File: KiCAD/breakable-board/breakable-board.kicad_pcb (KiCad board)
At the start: 2 copper layers, 76.2 x 99.1 mm, 50 parts, among them J1 POWER1, J10 TQFP-32-2, J11 3.3V Out, J12 Power In, J13 5V Out, J14 GND, J15 SSOP-20-1, J16 SSOP-20-2, J17 I2C, J18 UART, J2 POWER3, J3 OUT1, J4 POWER2, J5 OUT3, J6 OUT2, J7 SOIC-14-1, J8 SOIC-14-2, J9 TQFP-32-1, SW1 Trigger, SW2 RESET, U1 LM555xN, U2 LM555xN, U3 LM555xN, U4 Package_SOIC-14, U5 Package_TQFP-32, U6 AMS1117-5.0, U7 AMS1117-3.3, U8 PIC16F1508-ISS

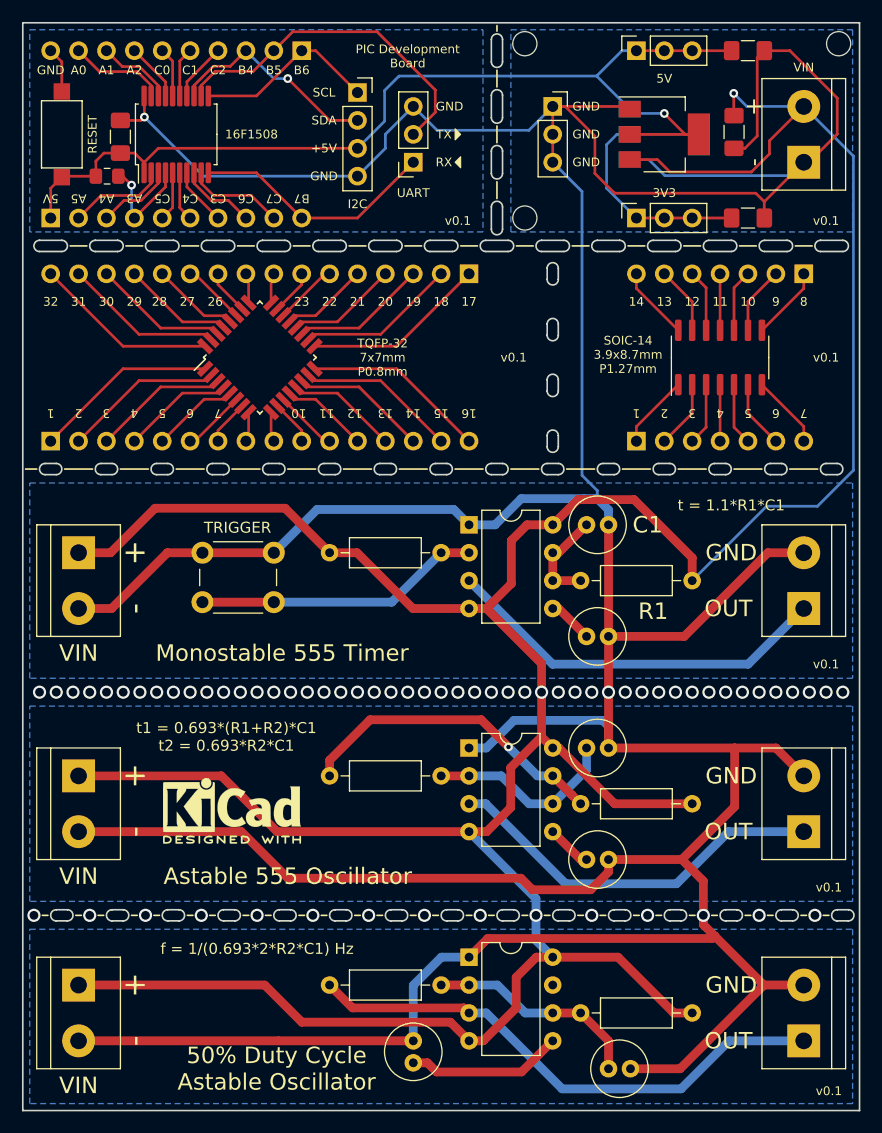
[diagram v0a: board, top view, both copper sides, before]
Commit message: Change hole size.
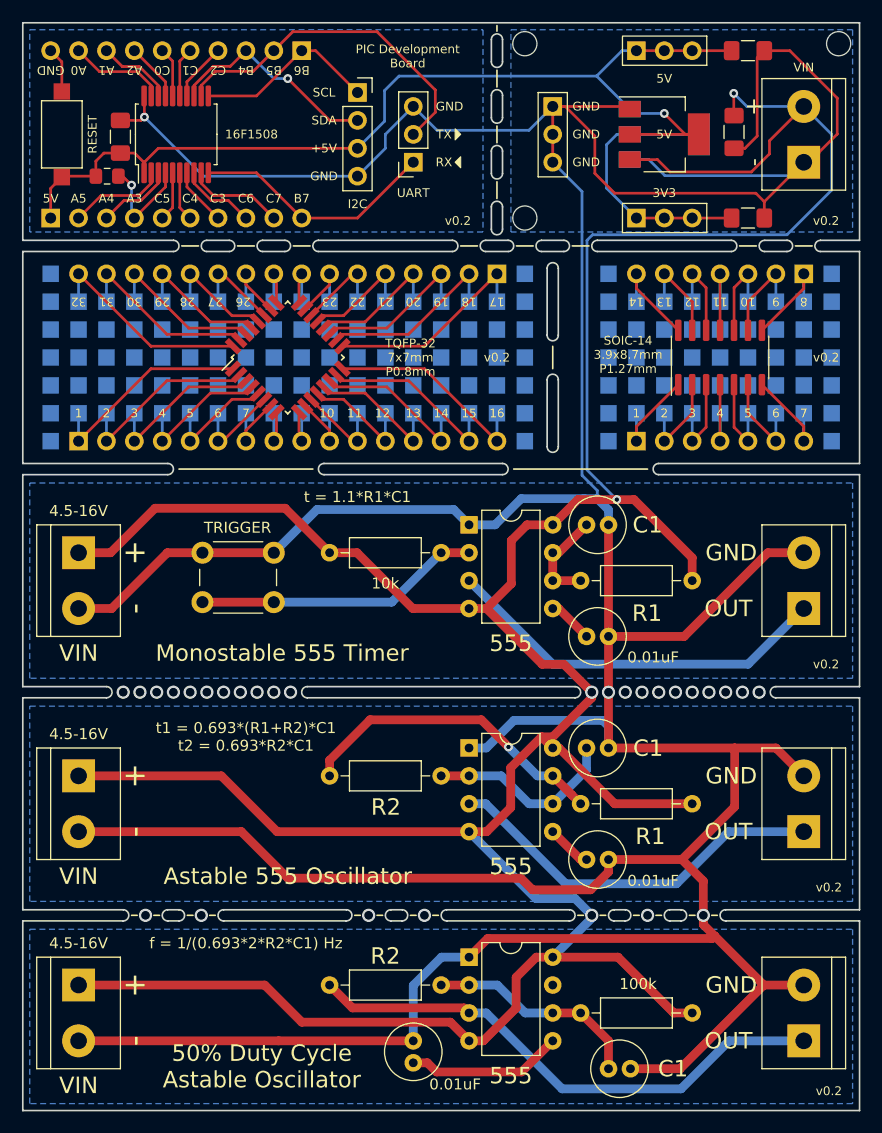
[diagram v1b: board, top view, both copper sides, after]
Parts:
- added .: ., TestPoint:TestPoint_Pad_1.5x1.5mm, B.Cu at (83.8, 58.4)
- added .: ., TestPoint:TestPoint_Pad_1.5x1.5mm, B.Cu at (91.4, 48.3)
- added .: ., TestPoint:TestPoint_Pad_1.5x1.5mm, B.Cu at (66.0, 53.3)
- added .: ., TestPoint:TestPoint_Pad_1.5x1.5mm, B.Cu at (66.0, 55.9)
- added .: ., TestPoint:TestPoint_Pad_1.5x1.5mm, B.Cu at (61.0, 53.3)
- added .: ., TestPoint:TestPoint_Pad_1.5x1.5mm, B.Cu at (58.4, 50.8)
- added .: ., TestPoint:TestPoint_Pad_1.5x1.5mm, B.Cu at (66.0, 50.8)
- added .: ., TestPoint:TestPoint_Pad_1.5x1.5mm, B.Cu at (63.5, 50.8)
- added .: ., TestPoint:TestPoint_Pad_1.5x1.5mm, B.Cu at (55.9, 55.9)
- added .: ., TestPoint:TestPoint_Pad_1.5x1.5mm, B.Cu at (58.4, 53.3)
- added .: ., TestPoint:TestPoint_Pad_1.5x1.5mm, B.Cu at (61.0, 55.9)
- added .: ., TestPoint:TestPoint_Pad_1.5x1.5mm, B.Cu at (63.5, 53.3)
- added .: ., TestPoint:TestPoint_Pad_1.5x1.5mm, B.Cu at (83.8, 48.3)
- added .: ., TestPoint:TestPoint_Pad_1.5x1.5mm, B.Cu at (58.4, 55.9)
- added .: ., TestPoint:TestPoint_Pad_1.5x1.5mm, B.Cu at (55.9, 53.3)
- added .: ., TestPoint:TestPoint_Pad_1.5x1.5mm, B.Cu at (61.0, 50.8)
- added .: ., TestPoint:TestPoint_Pad_1.5x1.5mm, B.Cu at (55.9, 50.8)
- added .: ., TestPoint:TestPoint_Pad_1.5x1.5mm, B.Cu at (50.8, 53.3)
- added .: ., TestPoint:TestPoint_Pad_1.5x1.5mm, B.Cu at (50.8, 55.9)
- added .: ., TestPoint:TestPoint_Pad_1.5x1.5mm, B.Cu at (53.3, 53.3)
- added .: ., TestPoint:TestPoint_Pad_1.5x1.5mm, B.Cu at (53.3, 55.9)
- added .: ., TestPoint:TestPoint_Pad_1.5x1.5mm, B.Cu at (53.3, 50.8)
- added .: ., TestPoint:TestPoint_Pad_1.5x1.5mm, B.Cu at (50.8, 50.8)
- added .: ., TestPoint:TestPoint_Pad_1.5x1.5mm, B.Cu at (94.0, 48.3)
- added .: ., TestPoint:TestPoint_Pad_1.5x1.5mm, B.Cu at (48.3, 53.3)
- added .: ., TestPoint:TestPoint_Pad_1.5x1.5mm, B.Cu at (45.7, 53.3)
- added .: ., TestPoint:TestPoint_Pad_1.5x1.5mm, B.Cu at (43.2, 50.8)
- added .: ., TestPoint:TestPoint_Pad_1.5x1.5mm, B.Cu at (45.7, 55.9)
- added .: ., TestPoint:TestPoint_Pad_1.5x1.5mm, B.Cu at (43.2, 55.9)
- added .: ., TestPoint:TestPoint_Pad_1.5x1.5mm, B.Cu at (43.2, 53.3)
- added .: ., TestPoint:TestPoint_Pad_1.5x1.5mm, B.Cu at (48.3, 50.8)
- added .: ., TestPoint:TestPoint_Pad_1.5x1.5mm, B.Cu at (48.3, 55.9)
- added .: ., TestPoint:TestPoint_Pad_1.5x1.5mm, B.Cu at (45.7, 50.8)
- added .: ., TestPoint:TestPoint_Pad_1.5x1.5mm, B.Cu at (40.6, 53.3)
- added .: ., TestPoint:TestPoint_Pad_1.5x1.5mm, B.Cu at (88.9, 48.3)
- added .: ., TestPoint:TestPoint_Pad_1.5x1.5mm, B.Cu at (40.6, 55.9)
- added .: ., TestPoint:TestPoint_Pad_1.5x1.5mm, B.Cu at (40.6, 50.8)
- added .: ., TestPoint:TestPoint_Pad_1.5x1.5mm, B.Cu at (38.1, 53.3)
- added .: ., TestPoint:TestPoint_Pad_1.5x1.5mm, B.Cu at (38.1, 50.8)
- added .: ., TestPoint:TestPoint_Pad_1.5x1.5mm, B.Cu at (38.1, 55.9)
- added .: ., TestPoint:TestPoint_Pad_1.5x1.5mm, B.Cu at (35.6, 55.9)
- added .: ., TestPoint:TestPoint_Pad_1.5x1.5mm, B.Cu at (33.0, 55.9)
- added .: ., TestPoint:TestPoint_Pad_1.5x1.5mm, B.Cu at (30.5, 55.9)
- added .: ., TestPoint:TestPoint_Pad_1.5x1.5mm, B.Cu at (30.5, 53.3)
- added .: ., TestPoint:TestPoint_Pad_1.5x1.5mm, B.Cu at (35.6, 53.3)
- added .: ., TestPoint:TestPoint_Pad_1.5x1.5mm, B.Cu at (86.4, 48.3)
- added .: ., TestPoint:TestPoint_Pad_1.5x1.5mm, B.Cu at (33.0, 53.3)
- added .: ., TestPoint:TestPoint_Pad_1.5x1.5mm, B.Cu at (35.6, 50.8)
- added .: ., TestPoint:TestPoint_Pad_1.5x1.5mm, B.Cu at (33.0, 50.8)
- added .: ., TestPoint:TestPoint_Pad_1.5x1.5mm, B.Cu at (30.5, 50.8)
- added .: ., TestPoint:TestPoint_Pad_1.5x1.5mm, B.Cu at (66.0, 58.4)
- added .: ., TestPoint:TestPoint_Pad_1.5x1.5mm, B.Cu at (58.4, 58.4)
- added .: ., TestPoint:TestPoint_Pad_1.5x1.5mm, B.Cu at (45.7, 58.4)
- added .: ., TestPoint:TestPoint_Pad_1.5x1.5mm, B.Cu at (68.6, 58.4)
- added .: ., TestPoint:TestPoint_Pad_1.5x1.5mm, B.Cu at (50.8, 58.4)
- added .: ., TestPoint:TestPoint_Pad_1.5x1.5mm, B.Cu at (91.4, 58.4)
- added .: ., TestPoint:TestPoint_Pad_1.5x1.5mm, B.Cu at (43.2, 58.4)
- added .: ., TestPoint:TestPoint_Pad_1.5x1.5mm, B.Cu at (48.3, 58.4)
- added .: ., TestPoint:TestPoint_Pad_1.5x1.5mm, B.Cu at (53.3, 58.4)
- added .: ., TestPoint:TestPoint_Pad_1.5x1.5mm, B.Cu at (33.0, 58.4)
- added .: ., TestPoint:TestPoint_Pad_1.5x1.5mm, B.Cu at (63.5, 58.4)
- added .: ., TestPoint:TestPoint_Pad_1.5x1.5mm, B.Cu at (61.0, 58.4)
- added .: ., TestPoint:TestPoint_Pad_1.5x1.5mm, B.Cu at (55.9, 58.4)
- added .: ., TestPoint:TestPoint_Pad_1.5x1.5mm, B.Cu at (40.6, 58.4)
- added .: ., TestPoint:TestPoint_Pad_1.5x1.5mm, B.Cu at (38.1, 58.4)
- added .: ., TestPoint:TestPoint_Pad_1.5x1.5mm, B.Cu at (30.5, 58.4)
- added .: ., TestPoint:TestPoint_Pad_1.5x1.5mm, B.Cu at (88.9, 58.4)
- added .: ., TestPoint:TestPoint_Pad_1.5x1.5mm, B.Cu at (35.6, 58.4)
- added .: ., TestPoint:TestPoint_Pad_1.5x1.5mm, B.Cu at (68.6, 48.3)
- added .: ., TestPoint:TestPoint_Pad_1.5x1.5mm, B.Cu at (45.7, 48.3)
- added .: ., TestPoint:TestPoint_Pad_1.5x1.5mm, B.Cu at (53.3, 48.3)
- added .: ., TestPoint:TestPoint_Pad_1.5x1.5mm, B.Cu at (50.8, 48.3)
- added .: ., TestPoint:TestPoint_Pad_1.5x1.5mm, B.Cu at (48.3, 48.3)
- added .: ., TestPoint:TestPoint_Pad_1.5x1.5mm, B.Cu at (43.2, 48.3)
- added .: ., TestPoint:TestPoint_Pad_1.5x1.5mm, B.Cu at (58.4, 48.3)
- added .: ., TestPoint:TestPoint_Pad_1.5x1.5mm, B.Cu at (66.0, 48.3)
- added .: ., TestPoint:TestPoint_Pad_1.5x1.5mm, B.Cu at (63.5, 48.3)
- added .: ., TestPoint:TestPoint_Pad_1.5x1.5mm, B.Cu at (94.0, 58.4)
- added .: ., TestPoint:TestPoint_Pad_1.5x1.5mm, B.Cu at (61.0, 48.3)
- added .: ., TestPoint:TestPoint_Pad_1.5x1.5mm, B.Cu at (55.9, 48.3)
- added .: ., TestPoint:TestPoint_Pad_1.5x1.5mm, B.Cu at (40.6, 48.3)
- added .: ., TestPoint:TestPoint_Pad_1.5x1.5mm, B.Cu at (38.1, 48.3)
- added .: ., TestPoint:TestPoint_Pad_1.5x1.5mm, B.Cu at (30.5, 48.3)
- added .: ., TestPoint:TestPoint_Pad_1.5x1.5mm, B.Cu at (35.6, 48.3)
- added .: ., TestPoint:TestPoint_Pad_1.5x1.5mm, B.Cu at (33.0, 48.3)
- added .: ., TestPoint:TestPoint_Pad_1.5x1.5mm, B.Cu at (78.7, 55.9)
- added .: ., TestPoint:TestPoint_Pad_1.5x1.5mm, B.Cu at (78.7, 50.8)
- added .: ., TestPoint:TestPoint_Pad_1.5x1.5mm, B.Cu at (78.7, 53.3)
- added .: ., TestPoint:TestPoint_Pad_1.5x1.5mm, B.Cu at (81.3, 58.4)
- added .: ., TestPoint:TestPoint_Pad_1.5x1.5mm, B.Cu at (78.7, 45.7)
- added .: ., TestPoint:TestPoint_Pad_1.5x1.5mm, B.Cu at (78.7, 48.3)
- added .: ., TestPoint:TestPoint_Pad_1.5x1.5mm, B.Cu at (78.7, 58.4)
- added .: ., TestPoint:TestPoint_Pad_1.5x1.5mm, B.Cu at (78.7, 61.0)
- added .: ., TestPoint:TestPoint_Pad_1.5x1.5mm, B.Cu at (99.1, 61.0)
- added .: ., TestPoint:TestPoint_Pad_1.5x1.5mm, B.Cu at (99.1, 58.4)
- added .: ., TestPoint:TestPoint_Pad_1.5x1.5mm, B.Cu at (99.1, 45.7)
- added .: ., TestPoint:TestPoint_Pad_1.5x1.5mm, B.Cu at (99.1, 48.3)
- added .: ., TestPoint:TestPoint_Pad_1.5x1.5mm, B.Cu at (99.1, 50.8)
- added .: ., TestPoint:TestPoint_Pad_1.5x1.5mm, B.Cu at (99.1, 53.3)
- added .: ., TestPoint:TestPoint_Pad_1.5x1.5mm, B.Cu at (96.5, 58.4)
- added .: ., TestPoint:TestPoint_Pad_1.5x1.5mm, B.Cu at (99.1, 55.9)
- added .: ., TestPoint:TestPoint_Pad_1.5x1.5mm, B.Cu at (96.5, 55.9)
- added .: ., TestPoint:TestPoint_Pad_1.5x1.5mm, B.Cu at (96.5, 53.3)
- added .: ., TestPoint:TestPoint_Pad_1.5x1.5mm, B.Cu at (96.5, 50.8)
- added .: ., TestPoint:TestPoint_Pad_1.5x1.5mm, B.Cu at (94.0, 55.9)
- added .: ., TestPoint:TestPoint_Pad_1.5x1.5mm, B.Cu at (94.0, 50.8)
- added .: ., TestPoint:TestPoint_Pad_1.5x1.5mm, B.Cu at (94.0, 53.3)
- added .: ., TestPoint:TestPoint_Pad_1.5x1.5mm, B.Cu at (88.9, 53.3)
- added .: ., TestPoint:TestPoint_Pad_1.5x1.5mm, B.Cu at (88.9, 55.9)
- added .: ., TestPoint:TestPoint_Pad_1.5x1.5mm, B.Cu at (91.4, 53.3)
- added .: ., TestPoint:TestPoint_Pad_1.5x1.5mm, B.Cu at (86.4, 58.4)
- added .: ., TestPoint:TestPoint_Pad_1.5x1.5mm, B.Cu at (91.4, 55.9)
- added .: ., TestPoint:TestPoint_Pad_1.5x1.5mm, B.Cu at (91.4, 50.8)
- added .: ., TestPoint:TestPoint_Pad_1.5x1.5mm, B.Cu at (88.9, 50.8)
- added .: ., TestPoint:TestPoint_Pad_1.5x1.5mm, B.Cu at (86.4, 53.3)
- added .: ., TestPoint:TestPoint_Pad_1.5x1.5mm, B.Cu at (83.8, 53.3)
- added .: ., TestPoint:TestPoint_Pad_1.5x1.5mm, B.Cu at (81.3, 50.8)
- added .: ., TestPoint:TestPoint_Pad_1.5x1.5mm, B.Cu at (83.8, 55.9)
- added .: ., TestPoint:TestPoint_Pad_1.5x1.5mm, B.Cu at (81.3, 55.9)
- added .: ., TestPoint:TestPoint_Pad_1.5x1.5mm, B.Cu at (81.3, 53.3)
- added .: ., TestPoint:TestPoint_Pad_1.5x1.5mm, B.Cu at (86.4, 50.8)
- added .: ., TestPoint:TestPoint_Pad_1.5x1.5mm, B.Cu at (81.3, 48.3)
- added .: ., TestPoint:TestPoint_Pad_1.5x1.5mm, B.Cu at (86.4, 55.9)
- added .: ., TestPoint:TestPoint_Pad_1.5x1.5mm, B.Cu at (83.8, 50.8)
- added .: ., TestPoint:TestPoint_Pad_1.5x1.5mm, B.Cu at (71.1, 61.0)
- added .: ., TestPoint:TestPoint_Pad_1.5x1.5mm, B.Cu at (71.1, 45.7)
- added .: ., TestPoint:TestPoint_Pad_1.5x1.5mm, B.Cu at (71.1, 48.3)
- added .: ., TestPoint:TestPoint_Pad_1.5x1.5mm, B.Cu at (71.1, 58.4)
- added .: ., TestPoint:TestPoint_Pad_1.5x1.5mm, B.Cu at (27.9, 61.0)
- added .: ., TestPoint:TestPoint_Pad_1.5x1.5mm, B.Cu at (27.9, 58.4)
- added .: ., TestPoint:TestPoint_Pad_1.5x1.5mm, B.Cu at (27.9, 45.7)
- added .: ., TestPoint:TestPoint_Pad_1.5x1.5mm, B.Cu at (27.9, 48.3)
- added .: ., TestPoint:TestPoint_Pad_1.5x1.5mm, B.Cu at (96.5, 48.3)
- added .: ., TestPoint:TestPoint_Pad_1.5x1.5mm, B.Cu at (27.9, 53.3)
- added .: ., TestPoint:TestPoint_Pad_1.5x1.5mm, B.Cu at (27.9, 55.9)
- added .: ., TestPoint:TestPoint_Pad_1.5x1.5mm, B.Cu at (27.9, 50.8)
- added .: ., TestPoint:TestPoint_Pad_1.5x1.5mm, B.Cu at (68.6, 55.9)
- added .: ., TestPoint:TestPoint_Pad_1.5x1.5mm, B.Cu at (71.1, 53.3)
- added .: ., TestPoint:TestPoint_Pad_1.5x1.5mm, B.Cu at (71.1, 55.9)
- added .: ., TestPoint:TestPoint_Pad_1.5x1.5mm, B.Cu at (71.1, 50.8)
- added .: ., TestPoint:TestPoint_Pad_1.5x1.5mm, B.Cu at (68.6, 50.8)
- added .: ., TestPoint:TestPoint_Pad_1.5x1.5mm, B.Cu at (68.6, 53.3)
- added .: ., TestPoint:TestPoint_Pad_1.5x1.5mm, B.Cu at (63.5, 55.9)
- REF**: moved to B.Cu
- moved REF** 14.6 mm to (33.0, 33.0)
- moved J9 2.54 mm to (30.5, 61.0)
- moved U5 2.54 mm to (49.5, 53.3)
- moved J10 2.54 mm to (68.6, 45.7)
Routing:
- net +9V: track 313.7 -> 328.0 mm, vias 3 -> 4
- net Net-(J9-Pad7): track 4.12 -> 6.66 mm
- net Net-(J9-Pad10): track 4.12 -> 6.66 mm
- net Net-(J9-Pad15): track 14.6 -> 17.1 mm
- net Net-(J10-Pad2): track 14.6 -> 17.1 mm
- net Net-(J10-Pad7): track 4.12 -> 6.66 mm
- net Net-(J10-Pad10): track 4.12 -> 6.66 mm
- net Net-(J9-Pad6): track 5.75 -> 8.29 mm
- net Net-(J10-Pad11): track 5.75 -> 8.29 mm
- net Net-(J9-Pad9): track 2.74 -> 5.28 mm
- net Net-(J9-Pad8): track 2.74 -> 5.28 mm
- net Net-(J10-Pad9): track 2.74 -> 5.28 mm
- net Net-(J10-Pad8): track 2.74 -> 5.28 mm
- net Net-(J9-Pad5): track 7.96 -> 10.5 mm
- net Net-(J9-Pad4): track 10.2 -> 12.7 mm
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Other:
- outline, holes or cut-outs redrawn
- board text added: "0.01uF"
- board text added: "100k"
- board text added: "10k"
- board text added: "14.08.2020 Bahtiyar Bayram"
- board text added: "4.5-16V"
- board text added: "555"
- board text added: "R2"
- board text added: "v0.2"
- board text removed: "v0.1"
